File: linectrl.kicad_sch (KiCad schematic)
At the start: 1 part, among them U2 LM358

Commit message: layout and replicate remaining lines
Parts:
- U2: footprint (none) -> Package_DIP:DIP-8_W7.62mm
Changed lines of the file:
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@@
 			)
 		)
-		(property "Footprint" ""
+		(property "Footprint" "Package_DIP:DIP-8_W7.62mm"
 			(at 153.67 95.25 0)
 			(hide yes)
@@
 			)
 		)
-		(property "Footprint" ""
+		(property "Footprint" "Package_DIP:DIP-8_W7.62mm"
 			(at 116.84 130.81 0)
 			(hide yes)
@@
 			)
 		)
-		(property "Footprint" ""
+		(property "Footprint" "Package_DIP:DIP-8_W7.62mm"
 			(at 120.65 95.25 0)
 			(hide yes)
@@
 				)
 				(path "/eb421281-26a1-483f-b39a-0425ec8eb8df/e134bfb4-8959-4249-a7dd-8912fc4b0eb6"
-					(page "10")
+					(page "11")
 				)
 				(path "/eb421281-26a1-483f-b39a-0425ec8eb8df/b0f9f7c2-daf3-42bc-b325-e20704d56b03"
-					(page "11")
+					(page "13")
 				)
 				(path "/eb421281-26a1-483f-b39a-0425ec8eb8df/0b0224b2-e87f-4eed-adc6-d3b2e3f746a5"
-					(page "12")
+					(page "15")
 				)
 			)
@@
 					(page "8")
 				)
-			)
+				(path "/eb421281-26a1-483f-b39a-0425ec8eb8df/e134bfb4-8959-4249-a7dd-8912fc4b0eb6"
+					(page "10")
+				)
+				(path "/eb421281-26a1-483f-b39a-0425ec8eb8df/b0f9f7c2-daf3-42bc-b325-e20704d56b03"
+					(page "12")
+				)
+				(path "/eb421281-26a1-483f-b39a-0425ec8eb8df/0b0224b2-e87f-4eed-adc6-d3b2e3f746a5"
+					(page "14")
+				)
+			)

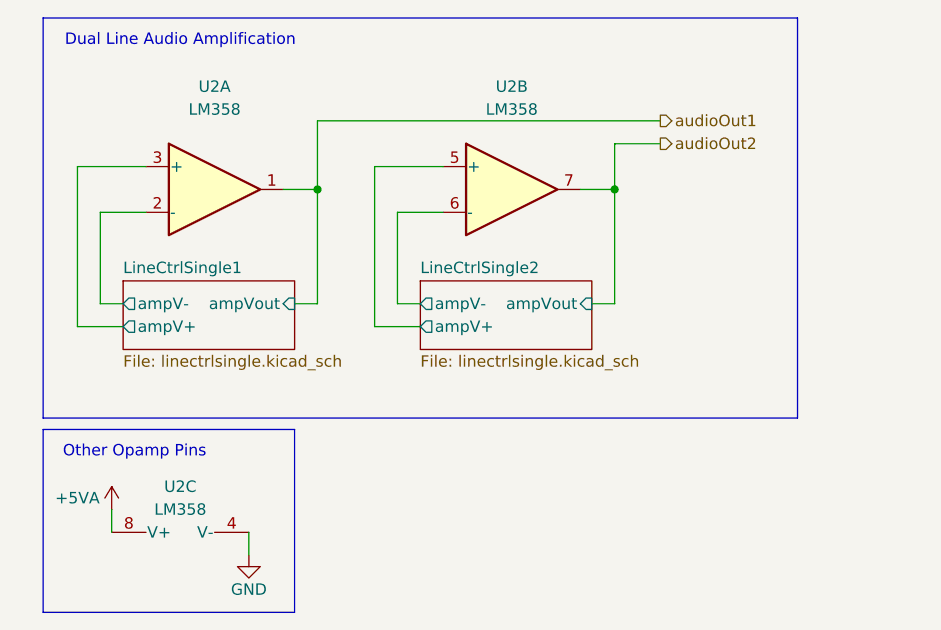
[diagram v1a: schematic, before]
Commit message: fix controlsw/hooksw subsheet error
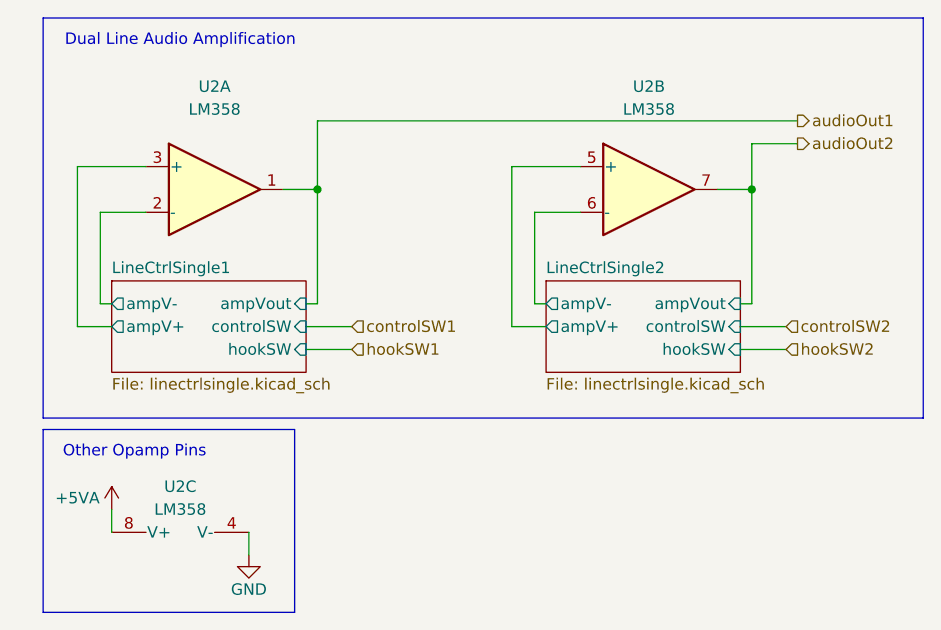
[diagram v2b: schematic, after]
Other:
- sheet LineCtrlSingle1 ports: added controlSW, hookSW; removed none
- sheet LineCtrlSingle2 ports: added controlSW, hookSW; removed none
- moved on the sheet: U2B
